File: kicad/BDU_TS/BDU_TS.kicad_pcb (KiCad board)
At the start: 2 copper layers, 83.7 x 60 mm, 16 parts, among them J10 Voltmeter-, J11 IMD-, J12 AIR-, J13 AIR+, J5 IMD+, J6 Voltmeter+, J7 TSAL_green+, J8 AIR+, J9 TSAL_green-

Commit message: BDU_TS
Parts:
- moved J12 72.7 mm to (156.8, 97.1), turned to -90 degrees
- moved J13 58.9 mm to (85.0, 113.8), turned to 90 degrees
- moved J8 50.8 mm to (85.2, 101.7), turned to 90 degrees
- moved J6 50.6 mm to (137.5, 124.5), turned to 180 degrees
- moved J9 49.0 mm to (133.1, 76.2), turned to 0 degrees
- moved F2 46.1 mm to (98.6, 115.2), turned to 0 degrees
- moved J10 45.5 mm to (123.8, 124.5), turned to 180 degrees
- moved R1 40.5 mm to (106.1, 115.5), turned to 90 degrees
- moved F10 31.9 mm to (98.1, 97.8), turned to -90 degrees
- moved J7 5.86 mm to (145.4, 76.3)

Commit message: bdu_ts update
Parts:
- moved J9 1.91 mm to (131.6, 75.0)
- moved J7 1.47 mm to (144.9, 75.0)
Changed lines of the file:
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@@
 			(psa4output no)
 			(plot_black_and_white yes)
-			(plotinvisibletext no)
 			(sketchpadsonfab no)
 			(plotpadnumbers no)
@@
 	(footprint "Connector_Molex:Molex_Micro-Fit_3.0_43650-0210_1x02-1MP_P3.00mm_Horizontal_PnP"
 		(layer "F.Cu")
-		(at 133.05 76.25)
+		(at 131.6 75)
 		(descr "Molex Micro-Fit 3.0 Connector System, 43650-0210 (compatible alternatives: 43650-0211, 43650-0209), 2 Pins per row (https://www.molex.com/pdm_docs/sd/436500210_sd.pdf), generated with kicad-footprint-generator")
 		(tags "connector Molex Micro-Fit_3.0 horizontal")
@@
 	(footprint "Connector_Molex:Molex_Micro-Fit_3.0_43650-0210_1x02-1MP_P3.00mm_Horizontal_PnP"
 		(layer "F.Cu")
-		(at 145.45 76.35)
+		(at 144.9 74.985)
 		(descr "Molex Micro-Fit 3.0 Connector System, 43650-0210 (compatible alternatives: 43650-0211, 43650-0209), 2 Pins per row (https://www.molex.com/pdm_docs/sd/436500210_sd.pdf), generated with kicad-footprint-generator")
 		(tags "connector Molex Micro-Fit_3.0 horizontal")

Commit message: Nicohlas sanity gone
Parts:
- moved J8 4.16 mm to (85.0, 97.5)
- moved F2 4.15 mm to (98.7, 111.1)
- moved R1 4.15 mm to (106.2, 111.3)
- moved F10 4.15 mm to (98.1, 93.6)
- moved J13 4.15 mm to (85.0, 109.6)
- moved J9 1.58 mm to (130.1, 75.5)
- moved J11 0.50 mm to (100.0, 75.5)
- moved J5 0.45 mm to (115.0, 75.5)
- moved J7 0.42 mm to (144.9, 75.4)
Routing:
- net TS-: track 0.00 -> 127.8 mm, vias 0 -> 4
- net /fused_TS+: track 0.00 -> 107.2 mm
- net TS+: track 3.00 -> 19.1 mm
- net /precharge: track 0.00 -> 9.06 mm
- net Net-(F2-Pad2): track 0.00 -> 5.16 mm

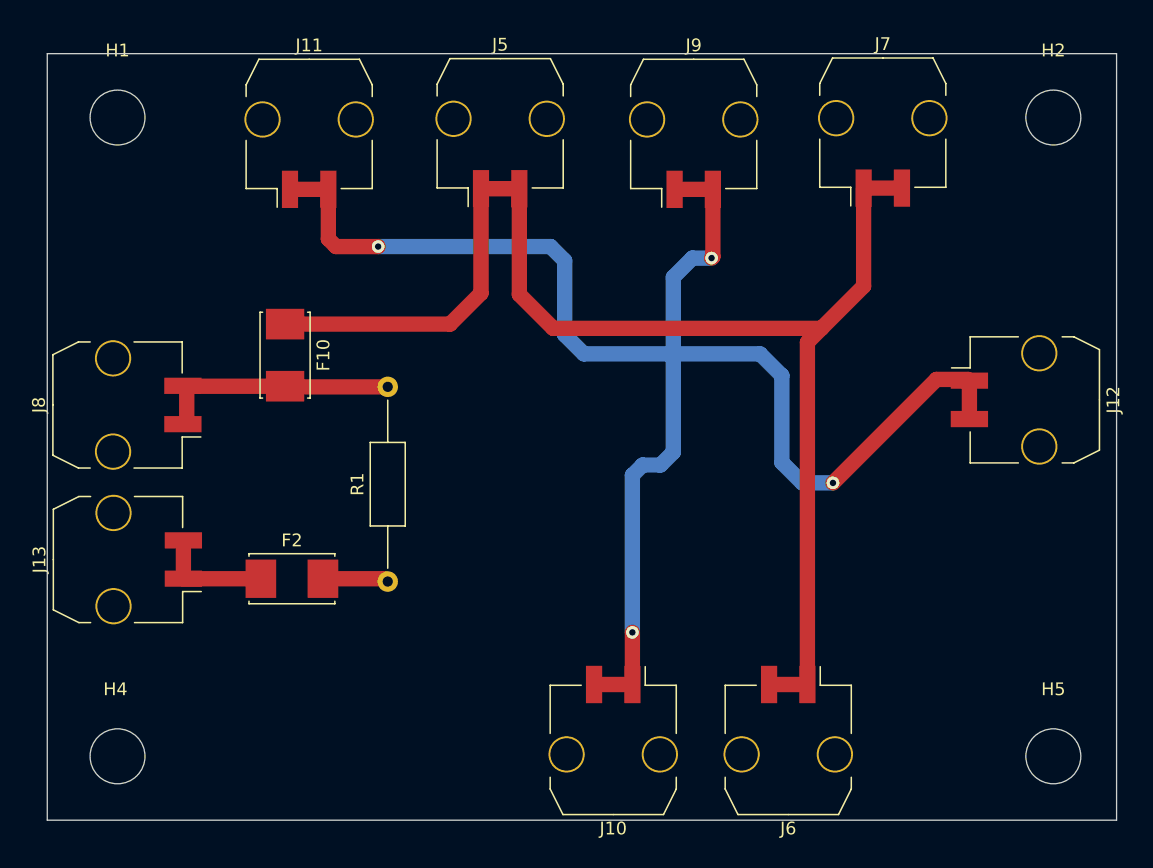
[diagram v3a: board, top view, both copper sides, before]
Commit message: BDU_TS and LVS v1 done
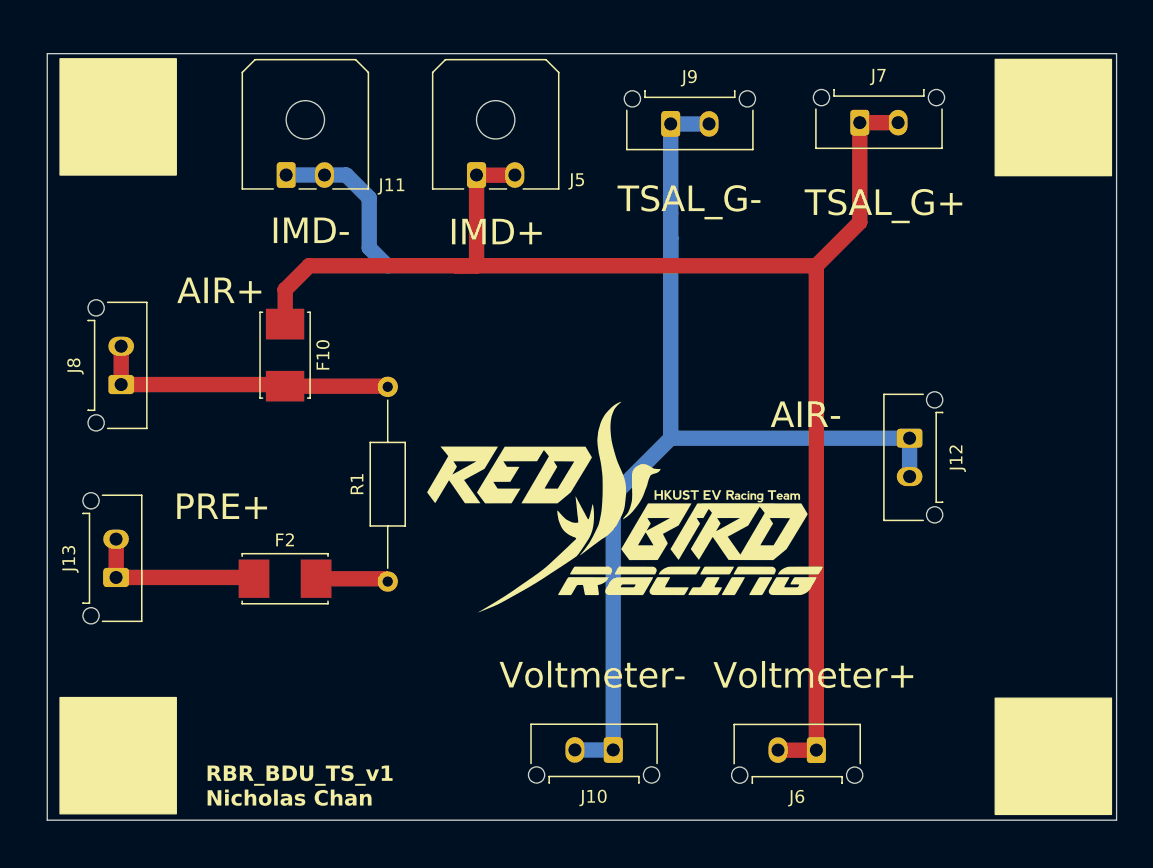
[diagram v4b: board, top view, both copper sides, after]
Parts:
- added G***: LOGO, RBR_logo:RBR_logo, F.Cu at (125.0, 105.4)
- J10, J12, J6, J7, J8, J9: footprint Connector_Molex:Molex_Micro-Fit_3.0_43650-0210_1x02-1MP_P3.00mm_Horizontal_PnP -> Connector_Molex:Molex_Micro-Fit_3.0_43650-0215_1x02_P3.00mm_Vertical
- J11, J5: footprint Connector_Molex:Molex_Micro-Fit_3.0_43650-0210_1x02-1MP_P3.00mm_Horizontal_PnP -> Connector_Molex:Molex_Micro-Fit_3.0_43650-0200_1x02_P3.00mm_Horizontal
- J13: value AIR+ -> PRE+; footprint Connector_Molex:Molex_Micro-Fit_3.0_43650-0210_1x02-1MP_P3.00mm_Horizontal_PnP -> Connector_Molex:Molex_Micro-Fit_3.0_43650-0215_1x02_P3.00mm_Vertical
- moved J12 10.2 mm to (147.0, 100.1)
- moved J5 4.45 mm to (113.1, 79.5)
- moved J11 4.39 mm to (98.2, 79.5)
- moved J6 2.20 mm to (139.7, 124.5)
- moved J7 1.80 mm to (143.1, 75.4)
- moved J9 1.80 mm to (128.3, 75.5)
- moved J8 1.63 mm to (85.3, 95.9)
- moved J13 1.41 mm to (84.9, 111.0)
- moved F2 0.54 mm to (98.1, 111.1)
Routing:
- net TS-: track 127.8 -> 116.1 mm, vias 4 -> 0
- net /fused_TS+: track 107.2 -> 113.3 mm
- net TS+: track 19.1 -> 23.9 mm
- net /precharge: track 9.06 -> 13.8 mm
- net Net-(F2-Pad2): track 5.16 -> 5.70 mm
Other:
- board text added: "AIR+"
- board text added: "AIR-"
- board text added: "IMD+"
- board text added: "IMD-"
- board text added: "PRE+"
- board text added: "RBR_BDU_TS_v1 Nicholas Chan"
- board text added: "TSAL_G+"
- board text added: "TSAL_G-"
- board text added: "Voltmeter+"
- board text added: "Voltmeter-"

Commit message: BDU _TS
resistor changed from board to external resistor
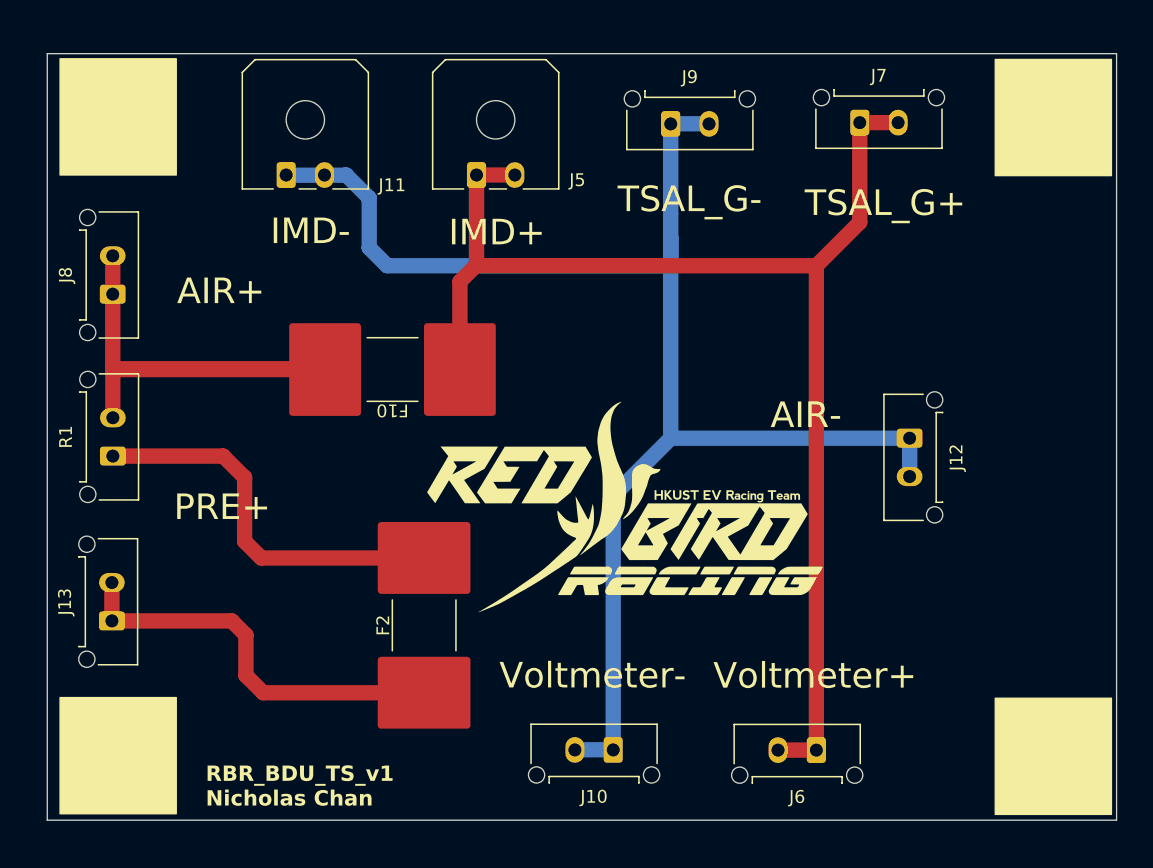
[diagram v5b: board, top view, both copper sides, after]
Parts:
- F10, F2: footprint Fuse:Fuseholder_Littelfuse_Nano2_157x -> Fuse:Fuse_Littelfuse-NANO2-885
- R1: footprint Resistor_THT:R_Axial_DIN0207_L6.3mm_D2.5mm_P15.24mm_Horizontal -> Connector_Molex:Molex_Micro-Fit_3.0_43650-0215_1x02_P3.00mm_Vertical
- moved R1 23.7 mm to (84.6, 101.5)
- moved F2 11.5 mm to (109.0, 114.8), turned to 90 degrees
- moved F10 8.48 mm to (106.5, 94.7), turned to 180 degrees
- moved J8 7.11 mm to (84.6, 88.8)
- moved J13 3.42 mm to (84.6, 114.4)
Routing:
- net Net-(F2-Pad2): track 5.70 -> 30.6 mm
- net TS+: track 23.9 -> 46.0 mm
- net /precharge: track 13.8 -> 31.6 mm
- net /fused_TS+: track 113.3 -> 101.9 mm

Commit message: BDU _TS gerbers
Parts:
- moved F10 1.30 mm to (107.8, 94.7)
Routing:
- net TS+: track 46.0 -> 50.8 mm
- net /fused_TS+: track 101.9 -> 101.4 mm
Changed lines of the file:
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@@
 			(psa4output no)
 			(plot_black_and_white yes)
-			(plotinvisibletext no)
 			(sketchpadsonfab no)
 			(plotpadnumbers no)
@@
 			(outputformat 1)
 			(mirror no)
-			(drillshape 1)
+			(drillshape 0)
 			(scaleselection 1)
-			(outputdirectory "")
+			(outputdirectory "./gerbers")
 		)
 	)
@@
 	(footprint "Fuse:Fuse_Littelfuse-NANO2-885"
 		(layer "F.Cu")
-		(at 106.525 94.725 180)
+		(at 107.825 94.725 180)
 		(descr "Littelfuse NANO2, 350VAC, 450/500VDC, 10.86 x 4.78 x 4.78mm, https://www.littelfuse.com/media?resourcetype=datasheets&itemid=888f12ed-ed3b-4b45-b910-06af8854ad76&filename=littelfuse-fuse-885-datasheet")
 		(tags "Fuse Nano2 885")
@@
 	)
 	(segment
-		(start 111.8 87.85)
-		(end 111.8 94.725)
-		(width 1.2)
-		(layer "F.Cu")
-		(net 3)
-	)
-	(segment
 		(start 139.7 86.6)
 		(end 143.1 83.2)
@@
 	)
 	(segment
-		(start 113.1 86.55)
-		(end 111.8 87.85)
-		(width 1.2)
-		(layer "F.Cu")
-		(net 3)
-	)
-	(segment
 		(start 113.15 86.6)
 		(end 139.7 86.6)
@@
 	)
 	(segment
+		(start 113.1 86.55)
+		(end 113.1 94.725)
+		(width 1.2)
+		(layer "F.Cu")
+		(net 3)
+	)
+	(segment
 		(start 84.625 88.825)
 		(end 84.625 94.725)
@@
 	)
 	(segment
+		(start 97.8 94.675)
+		(end 101.2 94.675)
+		(width 1.2)
+		(layer "F.Cu")
+		(net 4)
+	)
+	(segment
 		(start 101.2 94.675)
 		(end 101.25 94.725)
@@
 	(segment
 		(start 84.635 94.675)
-		(end 101.2 94.675)
+		(end 97.8 94.675)
 		(width 1.2)
 		(layer "F.Cu")
@@
 	)
 	(segment
+		(start 97.8 94.675)
+		(end 97.85 94.725)
+		(width 1.2)
+		(layer "F.Cu")
+		(net 4)
+	)
+	(segment
+		(start 97.85 94.725)
+		(end 102.55 94.725)
+		(width 1.2)
+		(layer "F.Cu")
+		(net 4)
+	)
+	(segment
 		(start 84.635 98.5)
 		(end 84.635 94.675)
@@
 	)
 	(segment
-		(start 128.3 84.4)
-		(end 128.3 82.5)
-		(width 1.2)
-		(layer "B.Cu")
-		(net 5)
-	)
-	(segment
 		(start 123.8 104.6)
 		(end 128.3 100.1)
@@
 	)
 	(segment
-		(start 128.3 82.5)
+		(start 128.3 84.4)
 		(end 128.3 75.5)
 		(width 1.2)
